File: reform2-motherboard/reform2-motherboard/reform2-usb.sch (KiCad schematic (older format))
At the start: 92 parts, among them J14 USB_INT2, J15 Conn_01x06_Male, J16 Conn_01x06_Male, J17 USB3_A, J5 USB3_A, J6 USB3_A, J9 USB_INT1, U15 TPS2561, U16 TPS2561, U9 TUSB8041, Y1 24MHz

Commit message: WIP: reform2 motherboard: more schematics tuning, preliminary selection of most components
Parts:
- C20, C21: Manufacturer (none) -> Yageo; Manufacturer_No (none) -> CC0603JRNPO9BN180
- C39, C40, C41, C42, C44, C45, C80, C82: Manufacturer (none) -> TDK; Manufacturer_No (none) -> CGA3E2X8R1E104K080AE
- C43: Manufacturer (none) -> Taiyo Yuden; Manufacturer_No (none) -> LMK107BBJ106KALT
- C66, C67, C70, C73, C74, C75, C76, C77, C84, C85, C86, C87, C88, C89, C90, C92, C93, C94, C95, C96, C97: footprint (none) -> Capacitor_SMD:C_0603_1608Metric; Manufacturer (none) -> TDK; Manufacturer_No (none) -> CGA3E2X8R1E104K080AE
- C68, C78, C79: value 0.001uF -> 1nF; footprint (none) -> Capacitor_SMD:C_0603_1608Metric; Manufacturer (none) -> KEMET; Manufacturer_No (none) -> C0603C102J5RACAUTO
- C69, C71, C72, C81, C83: value 150uF -> 220uF; footprint (none) -> Capacitor_SMD:CP_Elec_8x10; Manufacturer (none) -> Panasonic; Manufacturer_No (none) -> EEE-FT1H221GP
- C91, C98: footprint (none) -> Capacitor_SMD:C_0603_1608Metric; Manufacturer (none) -> Taiyo Yuden; Manufacturer_No (none) -> LMK107BBJ106KALT
- J14, J9: Manufacturer (none) -> 3M; Manufacturer_No (none) -> 951104-7622-AR
- J15, J16: footprint (none) -> Connector_PinSocket_2.54mm:PinSocket_1x06_P2.54mm_Vertical; Manufacturer (none) -> TE; Manufacturer_No (none) -> 826936-6
- J17, J5, J6: Manufacturer (none) -> Molex; Manufacturer_No (none) -> 48393-001
- R100, R101, R103, R82, R83, R88, R89, R94, R95, R98: footprint (none) -> Resistor_SMD:R_0603_1608Metric; Manufacturer (none) -> Vishay Dale; Manufacturer_No (none) -> CRCW06030000Z0EAC
- R102: value 1k -> 1.5k; footprint (none) -> Resistor_SMD:R_0603_1608Metric; Manufacturer (none) -> Yageo; Manufacturer_No (none) -> RC0603FR-071K5L
- R41, R55, R96, R97: Manufacturer (none) -> Yageo; Manufacturer_No (none) -> RC0603FR-071ML
- R57: Manufacturer (none) -> Yageo; Manufacturer_No (none) -> RC0603FR-079K53L
- R58, R59, R60, R63: Manufacturer (none) -> Yageo; Manufacturer_No (none) -> RC0603FR-074K7L
- R61: Manufacturer (none) -> Vishay Dale; Manufacturer_No (none) -> CRCW060390K9FKEAC
- R62: Manufacturer (none) -> Yageo; Manufacturer_No (none) -> AF0603JR-0710KL
- R81, R84, R85, R86: footprint (none) -> Resistor_SMD:R_0603_1608Metric; Manufacturer (none) -> Vishay Dale; Manufacturer_No (none) -> CRCW060310K0JNEAC
- R87, R90, R91, R92, R93, R99: footprint (none) -> Resistor_SMD:R_0603_1608Metric
- U15, U16: Manufacturer (none) -> Texas Instruments; Manufacturer_No (none) -> TPS2561
- U9: Manufacturer (none) -> Texas Instruments; Manufacturer_No (none) -> TUSB8041
- Y1: Manufacturer (none) -> Abracon; Manufacturer_No ABM8AIG -> ABM8AIG-24.000MHZ

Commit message: WIP: reform2 motherboard: rough placement
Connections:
- wire segments 275 -> 273
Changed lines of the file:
@@
 Connection ~ 11450 1750
-Wire Wire Line
-	11300 2300 11300 1950
-Wire Wire Line
-	11300 1950 11450 1950
-Connection ~ 11300 1950
-Wire Wire Line
-	11300 1950 11300 1750
-Connection ~ 11450 1950
 Wire Wire Line
 	11450 1950 11850 1950
@@
 	13050 2000 13050 1950
 Connection ~ 13050 1950
+Wire Wire Line
+	11300 1750 11300 2300
 $EndSCHEMATC

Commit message: WIP: reform 2 motherboard: tweaks for CL-SOM
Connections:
- wire segments 273 -> 275
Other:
- note added: "TODO: get rid of these?!"
- note removed: "TODO: wire up port power switches"
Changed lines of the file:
@@
 Sheet 3 9
 Title "MNT Reform 2 USB"
-Date "2019-07-03"
-Rev "0.1"
+Date "2019-07-09"
+Rev "0.1.1"
 Comp "MNT Research GmbH"
 Comment1 "https://mntre.com"
@@
 Wire Wire Line
 	9500 4800 9500 4750
-Text Notes 3750 10300 0    50   ~ 0
-TODO: wire up port power switches
 $Comp
 L Device:R_Small R60
@@
 Wire Wire Line
 	11300 1750 11300 2300
+Text GLabel 9000 1100 0    50   Input ~ 0
+USB_PWR
+$Comp
+L power:+5V #PWR0126
+U 1 1 5DBF4AD4
+P 9200 1000
+F 0 "#PWR0126" H 9200 850 50  0001 C CNN
+F 1 "+5V" H 9215 1173 50  0000 C CNN
+F 2 "" H 9200 1000 50  0001 C CNN
+F 3 "" H 9200 1000 50  0001 C CNN
+	1    9200 1000
+	1    0    0    -1
+$EndComp
+Wire Wire Line
+	9200 1000 9200 1100
+Wire Wire Line
+	9200 1100 9000 1100
+Text Notes 1350 8150 0    50   ~ 0
+TODO: get rid of these?!
 $EndSCHEMATC

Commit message: WIP: reform 2 motherboard: initial power section placement, routing tests
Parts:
- removed C69, C71, C72, C81, C83: 220uF, Capacitor_SMD:CP_Elec_8x10, symbol Device:CP_Small
- added C63, C69, C71, C72, C81: 10uF, Capacitor_SMD:C_0603_1608Metric, symbol Device:C_Small
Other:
- note added: "TODO: consider ESD7016"
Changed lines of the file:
@@
 Sheet 3 9
 Title "MNT Reform 2 USB"
-Date "2019-07-09"
-Rev "0.1.1"
+Date "2019-07-10"
+Rev "0.1.2"
 Comp "MNT Research GmbH"
 Comment1 "https://mntre.com"
@@
 	5500 5900 5550 5900
 $Comp
-L Device:CP_Small C69
-U 1 1 5DC97328
-P 2550 3550
-F 0 "C69" H 2638 3596 50  0000 L CNN
-F 1 "220uF" H 2638 3505 50  0000 L CNN
-F 2 "Capacitor_SMD:CP_Elec_8x10" H 2550 3550 50  0001 C CNN
-F 3 "~" H 2550 3550 50  0001 C CNN
-F 4 "Panasonic" H 2550 3550 50  0001 C CNN "Manufacturer"
-F 5 "EEE-FT1H221GP" H 2550 3550 50  0001 C CNN "Manufacturer_No"
-	1    2550 3550
-	1    0    0    -1
-$EndComp
-$Comp
 L Device:C_Small C70
 U 1 1 5DC98163
@@
 	2950 3700 2950 3650
 $Comp
-L Device:CP_Small C83
-U 1 1 5DCE097A
-P 6100 3550
-F 0 "C83" H 6188 3596 50  0000 L CNN
-F 1 "220uF" H 6188 3505 50  0000 L CNN
-F 2 "Capacitor_SMD:CP_Elec_8x10" H 6100 3550 50  0001 C CNN
-F 3 "~" H 6100 3550 50  0001 C CNN
-F 4 "Panasonic" H 6100 3550 50  0001 C CNN "Manufacturer"
-F 5 "EEE-FT1H221GP" H 6100 3550 50  0001 C CNN "Manufacturer_No"
-	1    6100 3550
-	1    0    0    -1
-$EndComp
-$Comp
 L Device:C_Small C85
 U 1 1 5DCE0984
@@
 	6500 3700 6500 3650
 $Comp
-L Device:CP_Small C71
-U 1 1 5DCED67A
-P 4700 8800
-F 0 "C71" H 4788 8846 50  0000 L CNN
-F 1 "220uF" H 4788 8755 50  0000 L CNN
-F 2 "Capacitor_SMD:CP_Elec_8x10" H 4700 8800 50  0001 C CNN
-F 3 "~" H 4700 8800 50  0001 C CNN
-F 4 "Panasonic" H 4700 8800 50  0001 C CNN "Manufacturer"
-F 5 "EEE-FT1H221GP" H 4700 8800 50  0001 C CNN "Manufacturer_No"
-	1    4700 8800
-	1    0    0    -1
-$EndComp
-$Comp
 L Device:C_Small C76
 U 1 1 5DCED684
@@
 	5100 8950 5100 8900
 $Comp
-L Device:CP_Small C72
-U 1 1 5DCFA988
-P 4700 9700
-F 0 "C72" H 4788 9746 50  0000 L CNN
-F 1 "220uF" H 4788 9655 50  0000 L CNN
-F 2 "Capacitor_SMD:CP_Elec_8x10" H 4700 9700 50  0001 C CNN
-F 3 "~" H 4700 9700 50  0001 C CNN
-F 4 "Panasonic" H 4700 9700 50  0001 C CNN "Manufacturer"
-F 5 "EEE-FT1H221GP" H 4700 9700 50  0001 C CNN "Manufacturer_No"
-	1    4700 9700
-	1    0    0    -1
-$EndComp
-$Comp
 L Device:C_Small C77
 U 1 1 5DCFA992
@@
 Wire Wire Line
 	3650 9550 4700 9550
-$Comp
-L Device:CP_Small C81
-U 1 1 5DDBD7E6
-P 6050 6050
-F 0 "C81" H 6138 6096 50  0000 L CNN
-F 1 "220uF" H 6138 6005 50  0000 L CNN
-F 2 "Capacitor_SMD:CP_Elec_8x10" H 6050 6050 50  0001 C CNN
-F 3 "~" H 6050 6050 50  0001 C CNN
-F 4 "Panasonic" H 6050 6050 50  0001 C CNN "Manufacturer"
-F 5 "EEE-FT1H221GP" H 6050 6050 50  0001 C CNN "Manufacturer_No"
-	1    6050 6050
-	1    0    0    -1
-$EndComp
 $Comp
 L Device:C_Small C84
@@
 Text Notes 1350 8150 0    50   ~ 0
 TODO: get rid of these?!
+$Comp
+L Device:C_Small C63
+U 1 1 5EEA2B4F
+P 2550 3550
+F 0 "C63" H 2642 3596 50  0000 L CNN
+F 1 "10uF" H 2642 3505 50  0000 L CNN
+F 2 "Capacitor_SMD:C_0603_1608Metric" H 2550 3550 50  0001 C CNN
+F 3 "~" H 2550 3550 50  0001 C CNN
+F 4 "TDK" H 2550 3550 50  0001 C CNN "Manufacturer"
+F 5 "CGA3E2X8R1E104K080AE" H 2550 3550 50  0001 C CNN "Manufacturer_No"
+	1    2550 3550
+	1    0    0    -1
+$EndComp
+$Comp
+L Device:C_Small C81
+U 1 1 5EEA2FE2
+P 6100 3550
+F 0 "C81" H 6192 3596 50  0000 L CNN
+F 1 "10uF" H 6192 3505 50  0000 L CNN
+F 2 "Capacitor_SMD:C_0603_1608Metric" H 6100 3550 50  0001 C CNN
+F 3 "~" H 6100 3550 50  0001 C CNN
+F 4 "TDK" H 6100 3550 50  0001 C CNN "Manufacturer"
+F 5 "CGA3E2X8R1E104K080AE" H 6100 3550 50  0001 C CNN "Manufacturer_No"
+	1    6100 3550
+	1    0    0    -1
+$EndComp
+$Comp
+L Device:C_Small C72
+U 1 1 5EEA3522
+P 6050 6050
+F 0 "C72" H 6142 6096 50  0000 L CNN
+F 1 "10uF" H 6142 6005 50  0000 L CNN
+F 2 "Capacitor_SMD:C_0603_1608Metric" H 6050 6050 50  0001 C CNN
+F 3 "~" H 6050 6050 50  0001 C CNN
+F 4 "TDK" H 6050 6050 50  0001 C CNN "Manufacturer"
+F 5 "CGA3E2X8R1E104K080AE" H 6050 6050 50  0001 C CNN "Manufacturer_No"
+	1    6050 6050
+	1    0    0    -1
+$EndComp
+$Comp
+L Device:C_Small C69
+U 1 1 5EEA41F9
+P 4700 8800
+F 0 "C69" H 4792 8846 50  0000 L CNN
+F 1 "10uF" H 4792 8755 50  0000 L CNN
+F 2 "Capacitor_SMD:C_0603_1608Metric" H 4700 8800 50  0001 C CNN
+F 3 "~" H 4700 8800 50  0001 C CNN
+F 4 "TDK" H 4700 8800 50  0001 C CNN "Manufacturer"
+F 5 "CGA3E2X8R1E104K080AE" H 4700 8800 50  0001 C CNN "Manufacturer_No"
+	1    4700 8800
+	1    0    0    -1
+$EndComp
+$Comp
+L Device:C_Small C71
+U 1 1 5EEA4792
+P 4700 9700
+F 0 "C71" H 4792 9746 50  0000 L CNN
+F 1 "10uF" H 4792 9655 50  0000 L CNN
+F 2 "Capacitor_SMD:C_0603_1608Metric" H 4700 9700 50  0001 C CNN
+F 3 "~" H 4700 9700 50  0001 C CNN
+F 4 "TDK" H 4700 9700 50  0001 C CNN "Manufacturer"
+F 5 "CGA3E2X8R1E104K080AE" H 4700 9700 50  0001 C CNN "Manufacturer_No"
+	1    4700 9700
+	1    0    0    -1
+$EndComp
+Text Notes 6300 7150 0    50   ~ 0
+TODO: consider ESD7016
 $EndSCHEMATC

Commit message: WIP: reform2 motherboard: USB3 hub routing
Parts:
- removed J15, J16: Conn_01x06_Male, Connector_PinSocket_2.54mm:PinSocket_1x06_P2.54mm_Vertical, symbol Connector:Conn_01x06_Male
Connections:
- net USB3_1_EN: now also R83.1; no longer R82.2
- net USB3_1_OVERCURn: now also R89.2; no longer R88.2
- net USB3_1_VBUS: now also U15.8 (OUT2); no longer U15.9 (OUT1)
- net USB3_2_EN: now also R82.2; no longer R83.1
- net USB3_2_OVERCURn: now also R88.2; no longer R89.2
- net USB3_2_VBUS: now also U15.9 (OUT1); no longer U15.8 (OUT2)
- net USB_SSTXP: now reaches C44.1, U9.55 (USB_SSTXP_UP)
- net USB_SSTXN: now reaches C45.1, U9.56 (USB_SSTXM_UP)
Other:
- note added: "TODO: terminate unused superspeeds?"
- note removed: "TODO: get rid of these?!"
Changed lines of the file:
@@
 Text GLabel 3700 3400 2    50   Input ~ 0
 USB3_1_VBUS
+Text GLabel 2900 1800 2    50   Output ~ 0
+USB3_1_VBUS
 Text GLabel 2900 1500 2    50   Output ~ 0
-USB3_1_VBUS
-Text GLabel 2900 1800 2    50   Output ~ 0
 USB3_2_VBUS
 $Comp
@@
 	4900 1600 4900 1500
 Connection ~ 4900 1500
+Text GLabel 1200 1800 0    50   Input ~ 0
+USB3_2_EN
 Text GLabel 1200 1900 0    50   Input ~ 0
-USB3_2_EN
-Text GLabel 1200 1800 0    50   Input ~ 0
 USB3_1_EN
 Text GLabel 4550 1900 0    50   Input ~ 0
@@
 Wire Wire Line
 	3700 9750 3650 9750
-Text GLabel 1850 8600 2    50   Output ~ 0
-USB3_3_SSTXP
-Text GLabel 1850 8700 2    50   Output ~ 0
-USB3_3_SSTXN
-Text GLabel 1850 8800 2    50   Output ~ 0
-USB3_3_SSRXP
-Text GLabel 1850 8900 2    50   Output ~ 0
-USB3_3_SSRXN
-Text GLabel 1850 9600 2    50   Output ~ 0
-USB3_4_SSTXP
-Text GLabel 1850 9700 2    50   Output ~ 0
-USB3_4_SSTXN
-Text GLabel 1850 9800 2    50   Output ~ 0
-USB3_4_SSRXP
-Text GLabel 1850 9900 2    50   Output ~ 0
-USB3_4_SSRXN
-$Comp
-L Connector:Conn_01x06_Male J15
-U 1 1 5D9A256D
-P 1400 8700
-F 0 "J15" H 1508 9081 50  0000 C CNN
-F 1 "Conn_01x06_Male" H 1508 8990 50  0000 C CNN
-F 2 "Connector_PinSocket_2.54mm:PinSocket_1x06_P2.54mm_Vertical" H 1400 8700 50  0001 C CNN
-F 3 "~" H 1400 8700 50  0001 C CNN
-F 4 "TE" H 1400 8700 50  0001 C CNN "Manufacturer"
-F 5 "826936-6" H 1400 8700 50  0001 C CNN "Manufacturer_No"
-	1    1400 8700
-	1    0    0    -1
-$EndComp
-$Comp
-L Connector:Conn_01x06_Male J16
-U 1 1 5D9A6768
-P 1400 9700
-F 0 "J16" H 1508 10081 50  0000 C CNN
-F 1 "Conn_01x06_Male" H 1508 9990 50  0000 C CNN
-F 2 "Connector_PinSocket_2.54mm:PinSocket_1x06_P2.54mm_Vertical" H 1400 9700 50  0001 C CNN
-F 3 "~" H 1400 9700 50  0001 C CNN
-F 4 "TE" H 1400 9700 50  0001 C CNN "Manufacturer"
-F 5 "826936-6" H 1400 9700 50  0001 C CNN "Manufacturer_No"
-	1    1400 9700
-	1    0    0    -1
-$EndComp
-Wire Wire Line
-	1850 8600 1600 8600
-Wire Wire Line
-	1600 8700 1850 8700
-Wire Wire Line
-	1850 8800 1600 8800
-Wire Wire Line
-	1600 8900 1850 8900
-Wire Wire Line
-	1850 9600 1600 9600
-Wire Wire Line
-	1600 9700 1850 9700
-Wire Wire Line
-	1850 9800 1600 9800
-Wire Wire Line
-	1600 9900 1850 9900
-$Comp
-L power:GND #PWR0197
-U 1 1 5D9CE045
-P 1650 9000
-F 0 "#PWR0197" H 1650 8750 50  0001 C CNN
-F 1 "GND" H 1655 8827 50  0000 C CNN
-F 2 "" H 1650 9000 50  0001 C CNN
-F 3 "" H 1650 9000 50  0001 C CNN
-	1    1650 9000
-	1    0    0    -1
-$EndComp
-Wire Wire Line
-	1600 9000 1650 9000
-$Comp
-L power:GND #PWR0198
-U 1 1 5D9D77BB
-P 1650 10000
-F 0 "#PWR0198" H 1650 9750 50  0001 C CNN
-F 1 "GND" H 1655 9827 50  0000 C CNN
-F 2 "" H 1650 10000 50  0001 C CNN
-F 3 "" H 1650 10000 50  0001 C CNN
-	1    1650 10000
-	1    0    0    -1
-$EndComp
-Wire Wire Line
-	1650 10000 1600 10000
-Text GLabel 1600 9500 2    50   Input ~ 0
-USB3_4_VBUS
-Text GLabel 1600 8500 2    50   Input ~ 0
-USB3_3_VBUS
 $Comp
 L Connector:USB3_A J17
@@
 Text GLabel 13500 6200 2    50   Input ~ 0
 USB3_4_OVERCURn
+Text GLabel 3100 1900 2    50   Output ~ 0
+USB3_1_OVERCURn
 Text GLabel 3100 1600 2    50   Output ~ 0
-USB3_1_OVERCURn
-Text GLabel 3100 1900 2    50   Output ~ 0
 USB3_2_OVERCURn
 Text GLabel 2100 6700 2    50   Output ~ 0
@@
 Wire Wire Line
 	9200 1100 9000 1100
-Text Notes 1350 8150 0    50   ~ 0
-TODO: get rid of these?!
 $Comp
 L Device:C_Small C63
@@
 Text Notes 6300 7150 0    50   ~ 0
 TODO: consider ESD7016
+Text Label 9850 3900 0    50   ~ 0
+USB_SSTXP
+Text Label 9850 4000 0    50   ~ 0
+USB_SSTXN
+Text Notes 14400 4750 0    50   ~ 0
+TODO: terminate unused superspeeds?
 $EndSCHEMATC

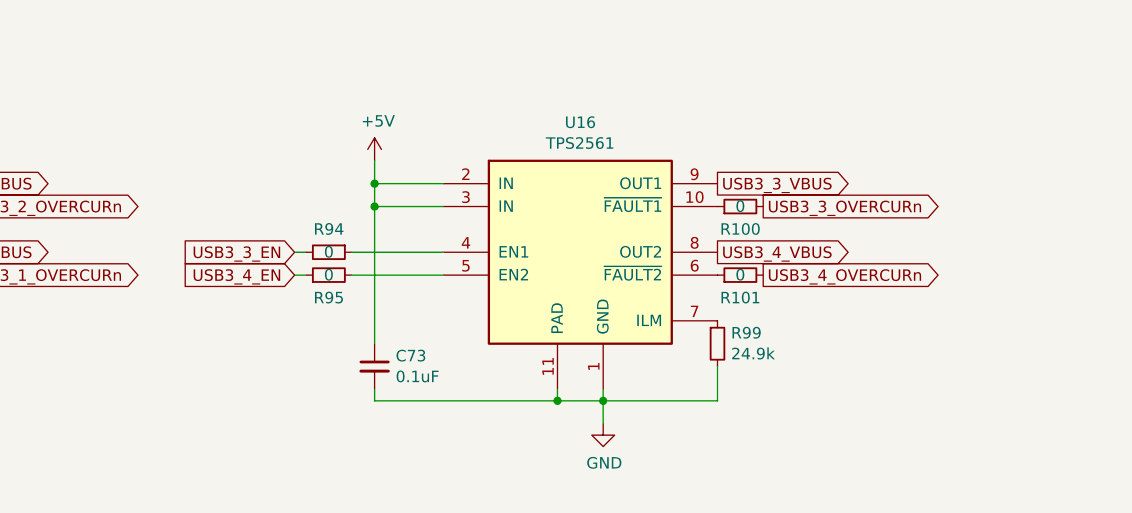
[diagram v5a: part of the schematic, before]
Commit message: WIP: reform2 motherboard: most of battery stuff routed, reshuffled
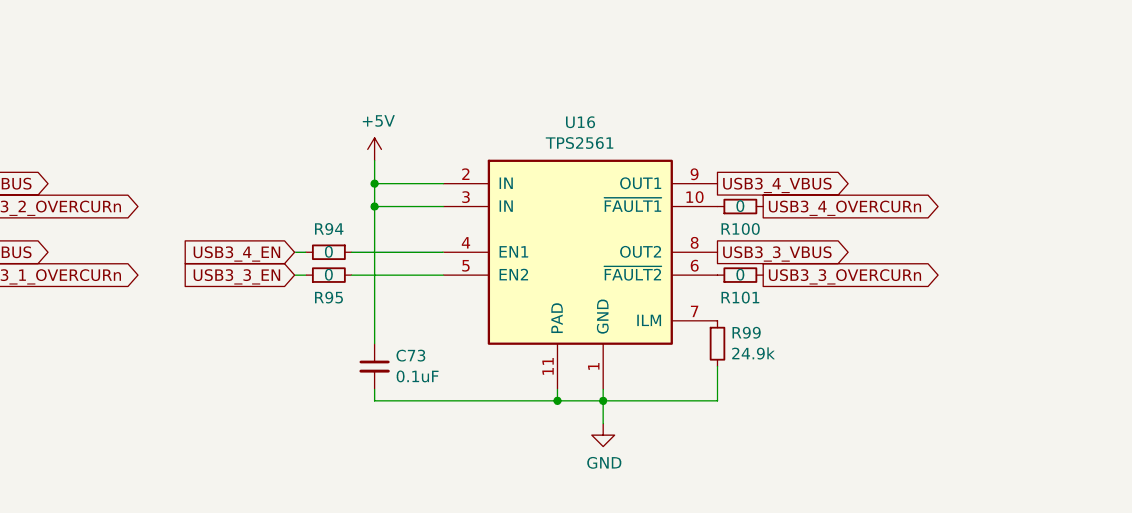
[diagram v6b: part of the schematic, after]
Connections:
- net USB3_3_EN: now also R95.1; no longer R94.2
- net USB3_3_OVERCURn: now also R101.2; no longer R100.2
- net USB3_3_VBUS: now also U16.8 (OUT2); no longer U16.9 (OUT1)
- net USB3_4_EN: now also R94.2; no longer R95.1
- net USB3_4_OVERCURn: now also R100.2; no longer R101.2
- net USB3_4_VBUS: now also U16.9 (OUT1); no longer U16.8 (OUT2)
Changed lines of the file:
@@
 Wire Wire Line
 	10000 3400 10650 3400
+Text GLabel 6400 1800 2    50   Output ~ 0
+USB3_3_VBUS
 Text GLabel 6400 1500 2    50   Output ~ 0
-USB3_3_VBUS
-Text GLabel 6400 1800 2    50   Output ~ 0
 USB3_4_VBUS
 $Comp
@@
 Text GLabel 1200 1900 0    50   Input ~ 0
 USB3_1_EN
+Text GLabel 4550 1800 0    50   Input ~ 0
+USB3_4_EN
 Text GLabel 4550 1900 0    50   Input ~ 0
-USB3_4_EN
-Text GLabel 4550 1800 0    50   Input ~ 0
 USB3_3_EN
 $Comp
@@
 Wire Wire Line
 	1550 6200 1800 6200
+Text GLabel 6600 1900 2    50   Output ~ 0
+USB3_3_OVERCURn
 Text GLabel 6600 1600 2    50   Output ~ 0
-USB3_3_OVERCURn
-Text GLabel 6600 1900 2    50   Output ~ 0
 USB3_4_OVERCURn
 $Comp

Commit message: reform2: first motherboard fully routed, checks TBD
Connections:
- net USB3_3_SSRXN: no longer names the net of U9.23 (USB_SSRXM_DN3)
- net USB3_3_SSRXP: no longer names the net of U9.22 (USB_SSRXP_DN3)
- net USB3_3_SSTXN: no longer names the net of U9.20 (USB_SSTXM_DN3)
- net USB3_3_SSTXP: no longer names the net of U9.19 (USB_SSTXP_DN3)
- net USB3_4_SSRXN: no longer names the net of U9.30 (USB_SSRXM_DN4)
- net USB3_4_SSRXP: no longer names the net of U9.29 (USB_SSRXP_DN4)
- net USB3_4_SSTXN: no longer names the net of U9.27 (USB_SSTXM_DN4)
- net USB3_4_SSTXP: no longer names the net of U9.26 (USB_SSTXP_DN4)
- no-connect marks 3 -> 11
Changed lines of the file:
@@
 Text GLabel 13500 4200 2    50   Output ~ 0
 USB3_2_DN
-Text GLabel 13500 4600 2    50   Output ~ 0
-USB3_3_SSTXP
-Text GLabel 13500 4700 2    50   Output ~ 0
-USB3_3_SSTXN
-Text GLabel 13500 4800 2    50   Output ~ 0
-USB3_3_SSRXP
-Text GLabel 13500 4900 2    50   Output ~ 0
-USB3_3_SSRXN
 Text GLabel 13500 5000 2    50   Output ~ 0
 USB3_3_DP
 Text GLabel 13500 5100 2    50   Output ~ 0
 USB3_3_DN
-Text GLabel 13500 5500 2    50   Output ~ 0
-USB3_4_SSTXP
-Text GLabel 13500 5600 2    50   Output ~ 0
-USB3_4_SSTXN
-Text GLabel 13500 5700 2    50   Output ~ 0
-USB3_4_SSRXP
-Text GLabel 13500 5800 2    50   Output ~ 0
-USB3_4_SSRXN
 Text GLabel 13500 5900 2    50   Output ~ 0
 USB3_4_DP
@@
 Text Notes 14400 4750 0    50   ~ 0
 TODO: terminate unused superspeeds?
+NoConn ~ 13500 4600
+NoConn ~ 13500 4700
+NoConn ~ 13500 4800
+NoConn ~ 13500 4900
+NoConn ~ 13500 5500
+NoConn ~ 13500 5600
+NoConn ~ 13500 5700
+NoConn ~ 13500 5800
 $EndSCHEMATC

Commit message: reform2 motherboard: pinout and footprint checks completed; ERC checks fixed 100%
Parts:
- R81, R84, R85, R86: value 10k -> 100k
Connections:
- net USB1_RX_N: now also U9.56 (USB_SSTXM_UP); no longer U9.59 (USB_SSRXM_UP)
- net USB1_RX_P: now also U9.55 (USB_SSTXP_UP); no longer U9.58 (USB_SSRXP_UP)
- net USB_SSTXN: now also U9.59 (USB_SSRXM_UP); no longer U9.56 (USB_SSTXM_UP)
- net USB_SSTXP: now also U9.58 (USB_SSRXP_UP); no longer U9.55 (USB_SSTXP_UP)
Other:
- moved on the sheet: C44, C45, FB1, FB2, R98
